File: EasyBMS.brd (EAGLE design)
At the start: 49 x 100 mm, 146 parts, among them Q10 BSS84LT1G, Q11 BSS84LT1G, Q12 BSS84LT1G, Q13 BSS84LT1G, Q2 BSS84LT1G, Q3 BSS84LT1G, Q4 BSS84LT1G, Q5 BSS84LT1G, Q6 BSS84LT1G, Q7 BSS84LT1G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

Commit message: restructured layout
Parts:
- removed JP6: (no value), pinhead:1X08
- added JP10, JP9: (no value), pinhead:1X02
- added JP8: (no value), pinhead:1X05
- JP4: device pinhead:1X08 -> pinhead:1X05
- moved JP4 60.4 mm to (-1.52, -3.81), turned to 0 degrees
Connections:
- removed net GPIO2: JP5.26
- removed net GPIO3: JP5.24
- new net ISIGNAL: JP5.24, JP8.3
- new net N$15: JP4.2
- new net N$17: JP4.3
- new net N$18: JP4.4
- new net N$25: JP4.5
- new net N$7: JP4.1
- net 5VDC: now also JP8.1, JP8.2
- net GND: now also JP10.1, JP10.2, JP8.4, JP8.5, JP9.1, JP9.2
- net GPIO1: no longer JP5.28
- net VTEMP1: now also JP5.28
- net VTEMP2: now also JP5.26

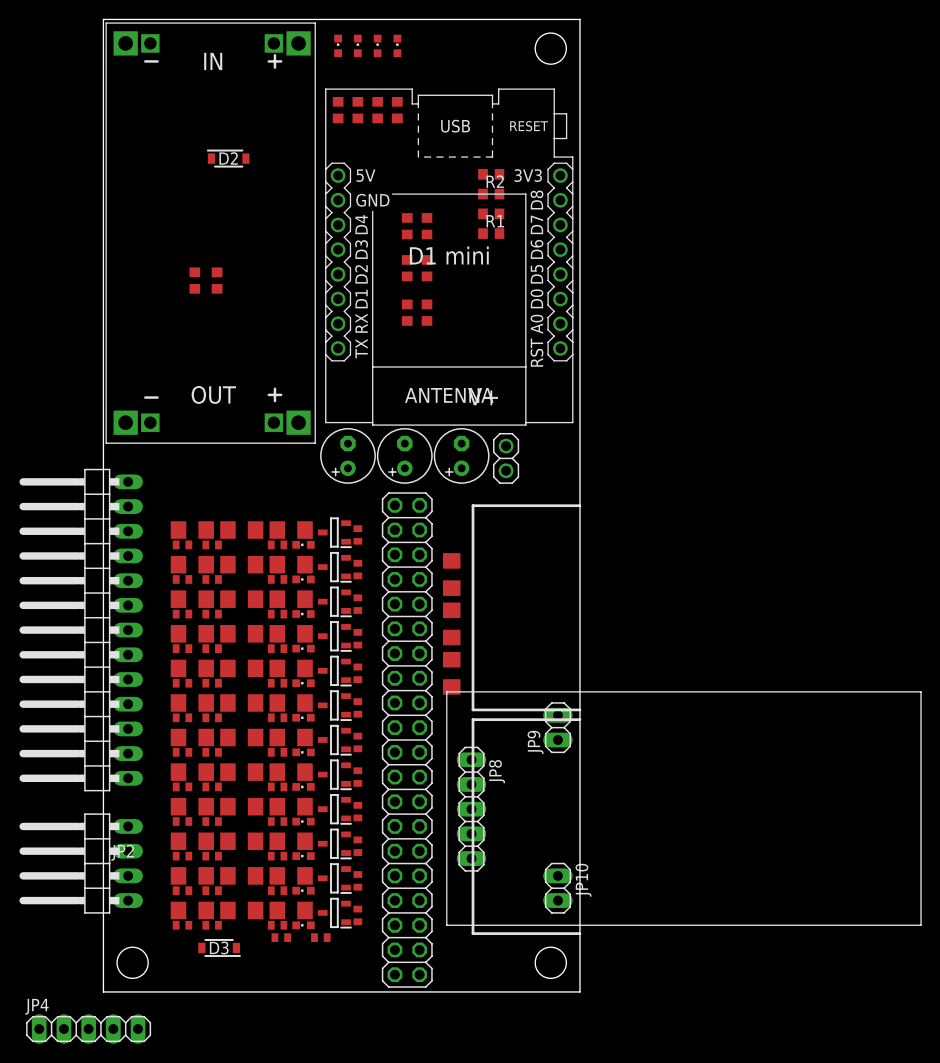
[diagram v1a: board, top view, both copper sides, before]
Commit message: new footprint for current sensor added
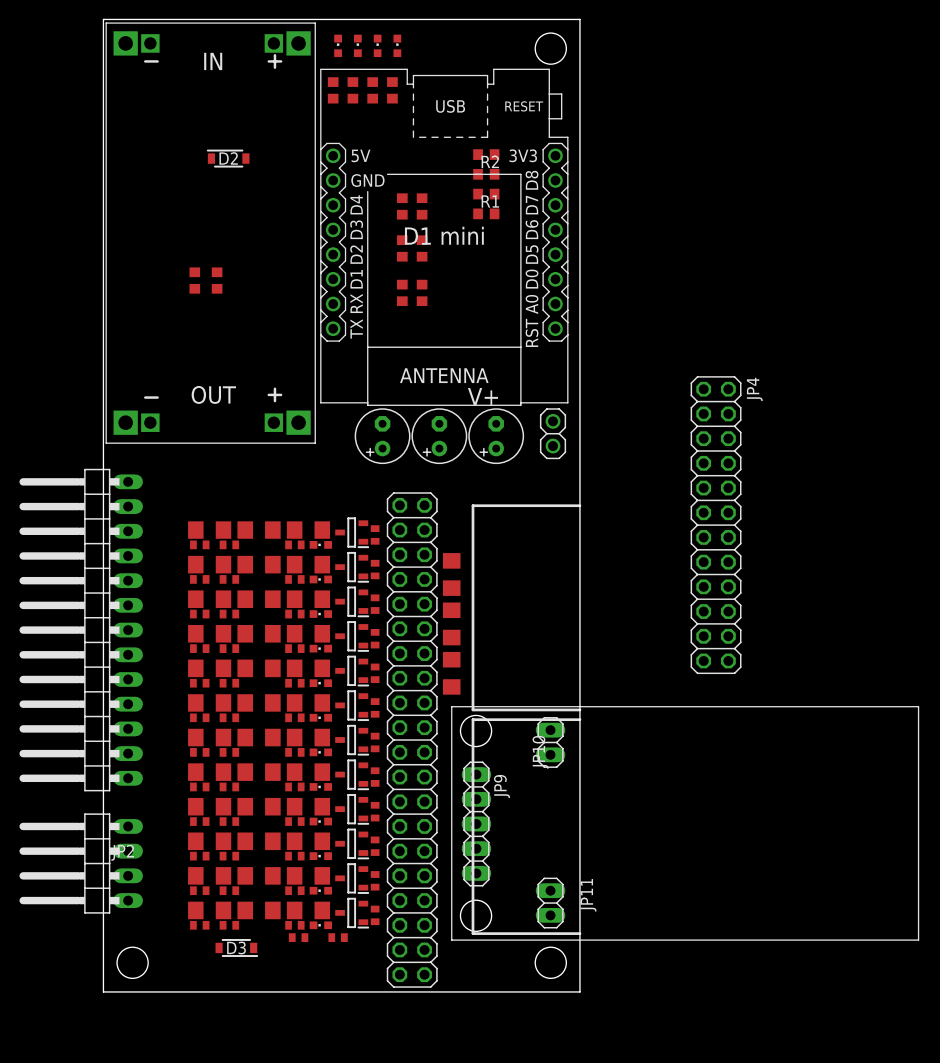
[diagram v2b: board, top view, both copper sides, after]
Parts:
- removed JP8: (no value), pinhead:1X05
- added JP11: (no value), pinhead:1X02
- JP4: device pinhead:1X05 -> pinhead:2X12
- JP9: device pinhead:1X02 -> pinhead:1X05
- moved JP4 82.7 mm to (63.0, 48.0), turned to 270 degrees
- moved JP10 15.0 mm to (46.0, 25.7), turned to 90 degrees
- moved JP9 13.0 mm to (38.4, 17.3), turned to 270 degrees
- moved JP3 5.45 mm to (46.2, 57.4)
- moved C3 4.10 mm to (40.4, 57.1)
- moved C1 4.10 mm to (28.7, 57.1)
- moved C2 4.10 mm to (34.5, 57.1)
- moved R1 2.09 mm to (39.4, 80.0)
- moved R15 2.09 mm to (32.8, 80.8)
- moved R5 2.09 mm to (32.8, 71.9)
- moved U$2 2.09 mm to (35.1, 77.7)
- moved R16 2.09 mm to (30.7, 80.8)
- moved R6 2.09 mm to (30.7, 71.9)
- moved R2 2.09 mm to (39.4, 84.1)
- moved R60 2.09 mm to (32.8, 76.5)
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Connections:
- removed net N$15: JP4.2
- removed net N$17: JP4.3
- removed net N$18: JP4.4
- removed net N$25: JP4.5
- removed net N$7: JP4.1
- net 5VDC: now also JP9.1, JP9.2; no longer JP8.1, JP8.2
- net GND: now also JP11.1, JP11.2, JP9.4, JP9.5; no longer JP8.4, JP8.5, JP9.1, JP9.2
- net ISIGNAL: now also JP9.3; no longer JP8.3

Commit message: layout finished
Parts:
- removed R5: 100R, rcl:R0603
- removed R59: 300k, rcl:R0603
- removed R6: 20k, rcl:R0603
- removed R60: 27k, rcl:R0603
- added C20: 100n, rcl:C0402
- added JP6: (no value), pinhead:2X05
- added R9: 100R, rcl:R0402
- C10, C11, C12, C13, C14, C15, C16, C17, C5, C6, C7, C8, C9: value (none) -> 10nF
- C18, C19, C4: value (none) -> 100nF
- JP4: device pinhead:2X12 -> pinhead:2X05
- R15: value 510k -> 470k
- moved JP2 37.1 mm to (-1.27, 50.3)
- moved JP3 31.5 mm to (15.0, 53.6), turned to 0 degrees
- moved JP4 17.9 mm to (45.2, 49.8)
- moved R58 16.0 mm to (9.65, 57.1)
- moved R57 16.0 mm to (11.7, 57.1)
- moved JP1 11.2 mm to (-1.27, 26.0)
- moved R15 7.37 mm to (37.8, 75.4)
- moved R16 7.37 mm to (35.8, 75.4)
- moved R53 6.35 mm to (30.0, 92.7)
- moved LED4 6.35 mm to (23.9, 97.3)
- moved LED1 5.84 mm to (30.0, 97.3)
- moved R56 5.84 mm to (23.9, 92.7)
- moved R3 3.78 mm to (20.6, 4.32), turned to 0 degrees
- moved R48 3.54 mm to (9.65, 23.4)
- moved R83 3.54 mm to (9.65, 37.6)
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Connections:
- removed net BAT+: R15.2, R59.2
- removed net GPIO1: R59.1, R60.2
- removed net ICMP: R6.1
- removed net IMB: R5.2
- removed net IPB: R5.1
- new net V+: C20.2, JP5.1, R9.1
- net C1: now also JP6.9
- net C10: now also JP4.3
- net C11: now also JP4.1
- net C12: now also JP4.10, JP4.2, JP4.4, JP4.6, JP4.8
- net C2: now also JP6.7
- net C3: now also JP6.5
- net C4: now also JP6.3
- net C5: now also JP6.1
- net C6: now also JP6.10, JP6.2, JP6.4, JP6.6, JP6.8
- net C7: now also JP4.9
- net C8: now also JP4.7
- net C9: now also JP4.5
- net GND: now also C20.1; no longer R6.2, R60.1
- net P13: now also R15.2, R9.2; no longer JP5.1
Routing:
- net P13: track 0.00 -> 148.5 mm, vias 0 -> 3
- net 5VDC: track 0.00 -> 145.4 mm, vias 0 -> 2
- net VTEMP2: track 0.00 -> 75.8 mm, vias 0 -> 3
- net VTEMP1: track 0.00 -> 74.5 mm, vias 0 -> 1
- net C3: track 0.00 -> 72.4 mm, vias 0 -> 1
- net C1: track 0.00 -> 72.0 mm, vias 0 -> 2
- net C2: track 0.00 -> 69.3 mm, vias 0 -> 3
- net VREF2: track 0.00 -> 68.5 mm, vias 0 -> 1
- net C4: track 0.00 -> 66.9 mm, vias 0 -> 2
- net GND: track 0.00 -> 65.1 mm, vias 0 -> 35
- net C5: track 0.00 -> 62.8 mm, vias 0 -> 1
- net C6: track 0.00 -> 61.8 mm, vias 0 -> 1
- net C12: track 0.00 -> 57.0 mm, vias 0 -> 1
- net C7: track 0.00 -> 56.2 mm, vias 0 -> 1
- net C8: track 0.00 -> 55.2 mm, vias 0 -> 1
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- added copper zone on layer 1, net GND
- added copper zone on layer 16, net GND

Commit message: layout changes
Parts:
- moved R3 4.02 mm to (16.8, 3.05), turned to 180 degrees
- moved C20 0.25 mm to (24.4, 51.6)
- moved C18 0.25 mm to (37.3, 37.6)
- moved C4 0.25 mm to (37.3, 32.5)
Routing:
- net C0: track 54.3 -> 29.3 mm
- net C1: track 72.0 -> 70.0 mm
- net S1: track 17.9 -> 19.6 mm
- net VTEMP2: track 75.8 -> 74.2 mm
- net C5: track 62.8 -> 64.3 mm
- net S7: track 12.4 -> 11.1 mm
- net S2: track 10.9 -> 12.0 mm
- net C4: track 66.9 -> 68.0 mm
- net S8: track 10.6 -> 9.54 mm
- net S9: track 9.30 -> 8.33 mm
- net C2: track 69.3 -> 70.3 mm
- net C6: track 61.8 -> 61.0 mm
- net S3: track 17.1 -> 17.8 mm
- net VREF2: track 68.5 -> 69.1 mm
- net S6: track 13.2 -> 12.7 mm
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
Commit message: new branch for meb
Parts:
- added JP22, JP23, JP24, JP25, JP26, JP27, JP28, JP29, JP30, JP31, JP32, JP33, JP34, JP35, JP36: (no value), pinhead_own:1X02
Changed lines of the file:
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@@
 <setting verticaltext="up"/>
 </settings>
-<grid distance="10" unitdist="mil" unit="mil" style="lines" multiple="1" display="yes" altdistance="5" altunitdist="mil" altunit="mil"/>
+<grid distance="1" unitdist="mm" unit="mm" style="lines" multiple="1" display="yes" altdistance="5" altunitdist="mil" altunit="mil"/>
 <layers>
 <layer number="1" name="Top" color="4" fill="1" visible="yes" active="yes"/>
@@
 </pass>
 </autorouter>
+<groups>
+<board_group name="STECKER"/>
+</groups>
 <elements>
 <element name="U$1" library="diy-modules" package="DC-DC-STEP-DOWN-LM2596HVS" value="DC-DC-STEP-DOWN-LM2596HVS" x="2.286" y="97.536" smashed="yes" rot="R270"/>
@@
 <element name="JP10" library="pinhead" library_urn="urn:adsk.eagle:library:325" package="1X02" package3d_urn="urn:adsk.eagle:package:22435/2" value="" x="45.974" y="25.654" smashed="yes" rot="R90">
 <attribute name="NAME" x="45.4152" y="23.0378" size="1.27" layer="25" ratio="10" rot="R90"/>
-<attribute name="POPULARITY" value="98" x="47.244" y="25.654" size="1.778" layer="27" rot="R90" display="off"/>
 <attribute name="VALUE" x="50.419" y="23.114" size="1.27" layer="27" rot="R90"/>
 </element>
 <element name="JP11" library="pinhead" library_urn="urn:adsk.eagle:library:325" package="1X02" package3d_urn="urn:adsk.eagle:package:22435/2" value="" x="45.974" y="9.144" smashed="yes" rot="R270">
 <attribute name="NAME" x="49.0728" y="11.7602" size="1.27" layer="25" ratio="10" rot="R270"/>
-<attribute name="POPULARITY" value="98" x="47.244" y="9.144" size="1.778" layer="27" rot="R270" display="off"/>
 <attribute name="VALUE" x="44.069" y="11.684" size="1.27" layer="27" rot="R270"/>
 </element>
@@
 <attribute name="NAME" x="25.019" y="52.197" size="1.27" layer="25" rot="R270"/>
 <attribute name="VALUE" x="22.479" y="52.197" size="1.27" layer="27" rot="R270"/>
+</element>
+<element name="JP22" library="pinhead_own" package="1X02" package3d_urn="urn:adsk.eagle:package:22435/2" value="" x="-5" y="-68" smashed="yes" rot="R180" grouprefs="STECKER">
+<attribute name="NAME" x="-2.3838" y="-69.8288" size="1.27" layer="25" ratio="10" rot="R180"/>
+<attribute name="VALUE" x="-2.46" y="-64.825" size="1.27" layer="27" rot="R180"/>
+</element>
+<element name="JP23" library="pinhead_own" package="1X02" package3d_urn="urn:adsk.eagle:package:22435/2" value="" x="-5" y="-71" smashed="yes" grouprefs="STECKER">
+<attribute name="NAME" x="-7.6162" y="-69.1712" size="1.27" layer="25" ratio="10"/>
+<attribute name="VALUE" x="-7.54" y="-74.175" size="1.27" layer="27"/>
+</element>
+<element name="JP24" library="pinhead_own" package="1X02" package3d_urn="urn:adsk.eagle:package:22435/2" value="" x="-5" y="-74" smashed="yes" grouprefs="STECKER">
+<attribute name="NAME" x="-7.6162" y="-72.1712" size="1.27" layer="25" ratio="10"/>
+<attribute name="VALUE" x="-7.54" y="-77.175" size="1.27" layer="27"/>
+</element>
+<element name="JP25" library="pinhead_own" package="1X02" package3d_urn="urn:adsk.eagle:package:22435/2" value="" x="-5" y="-77" smashed="yes" grouprefs="STECKER">
+<attribute name="NAME" x="-7.6162" y="-75.1712" size="1.27" layer="25" ratio="10"/>
+<attribute name="VALUE" x="-7.54" y="-80.175" size="1.27" layer="27"/>
+</element>
+<element name="JP26" library="pinhead_own" package="1X02" package3d_urn="urn:adsk.eagle:package:22435/2" value="" x="-5" y="-80" smashed="yes" grouprefs="STECKER">
+<attribute name="NAME" x="-7.6162" y="-78.1712" size="1.27" layer="25" ratio="10"/>
+<attribute name="VALUE" x="-7.54" y="-83.175" size="1.27" layer="27"/>
+</element>
+<element name="JP27" library="pinhead_own" package="1X02" package3d_urn="urn:adsk.eagle:package:22435/2" value="" x="-5" y="-83" smashed="yes" grouprefs="STECKER">
+<attribute name="NAME" x="-7.6162" y="-81.1712" size="1.27" layer="25" ratio="10"/>
+<attribute name="VALUE" x="-7.54" y="-86.175" size="1.27" layer="27"/>
+</element>
+<element name="JP28" library="pinhead_own" package="1X02" package3d_urn="urn:adsk.eagle:package:22435/2" value="" x="-5" y="-86" smashed="yes" grouprefs="STECKER">
+<attribute name="NAME" x="-7.6162" y="-84.1712" size="1.27" layer="25" ratio="10"/>
+<attribute name="VALUE" x="-7.54" y="-89.175" size="1.27" layer="27"/>
+</element>
+<element name="JP29" library="pinhead_own" package="1X02" package3d_urn="urn:adsk.eagle:package:22435/2" value="" x="-5" y="-89" smashed="yes" grouprefs="STECKER">
+<attribute name="NAME" x="-7.6162" y="-87.1712" size="1.27" layer="25" ratio="10"/>
+<attribute name="VALUE" x="-7.54" y="-92.175" size="1.27" layer="27"/>
+</element>
+<element name="JP30" library="pinhead_own" package="1X02" package3d_urn="urn:adsk.eagle:package:22435/2" value="" x="-5" y="-92" smashed="yes" grouprefs="STECKER">
+<attribute name="NAME" x="-7.6162" y="-90.1712" size="1.27" layer="25" ratio="10"/>
+<attribute name="VALUE" x="-7.54" y="-95.175" size="1.27" layer="27"/>
+</element>
+<element name="JP31" library="pinhead_own" package="1X02" package3d_urn="urn:adsk.eagle:package:22435/2" value="" x="-5" y="-95" smashed="yes" grouprefs="STECKER">
+<attribute name="NAME" x="-7.6162" y="-93.1712" size="1.27" layer="25" ratio="10"/>
+<attribute name="VALUE" x="-7.54" y="-98.175" size="1.27" layer="27"/>
+</element>
+<element name="JP32" library="pinhead_own" package="1X02" package3d_urn="urn:adsk.eagle:package:22435/2" value="" x="-5" y="-98" smashed="yes" grouprefs="STECKER">
+<attribute name="NAME" x="-7.6162" y="-96.1712" size="1.27" layer="25" ratio="10"/>
+<attribute name="VALUE" x="-7.54" y="-101.175" size="1.27" layer="27"/>
+</element>
+<element name="JP33" library="pinhead_own" package="1X02" package3d_urn="urn:adsk.eagle:package:22435/2" value="" x="-5" y="-101" smashed="yes" grouprefs="STECKER">
+<attribute name="NAME" x="-7.6162" y="-99.1712" size="1.27" layer="25" ratio="10"/>
+<attribute name="VALUE" x="-7.54" y="-104.175" size="1.27" layer="27"/>
+</element>
+<element name="JP34" library="pinhead_own" package="1X02" package3d_urn="urn:adsk.eagle:package:22435/2" value="" x="-5" y="-144" smashed="yes">
+<attribute name="NAME" x="-7.6162" y="-142.1712" size="1.27" layer="25" ratio="10"/>
+<attribute name="VALUE" x="-7.54" y="-147.175" size="1.27" layer="27"/>
+</element>
+<element name="JP35" library="pinhead_own" package="1X02" package3d_urn="urn:adsk.eagle:package:22435/2" value="" x="-5" y="-150" smashed="yes">
+<attribute name="NAME" x="-7.6162" y="-148.1712" size="1.27" layer="25" ratio="10"/>
+<attribute name="VALUE" x="-7.54" y="-153.175" size="1.27" layer="27"/>
+</element>
+<element name="JP36" library="pinhead_own" package="1X02" package3d_urn="urn:adsk.eagle:package:22435/2" value="" x="-5" y="-156" smashed="yes">
+<attribute name="NAME" x="-7.6162" y="-154.1712" size="1.27" layer="25" ratio="10"/>
+<attribute name="VALUE" x="-7.54" y="-159.175" size="1.27" layer="27"/>
 </element>
 </elements>
@@
 packages will not be understood (or retained) with this version.
 </note>
+<note version="9.5" severity="warning">
+Since Version 9.5, EAGLE supports persistent groups with
+schematics, and board files. Those persistent groups
+will not be understood (or retained) with this version.
+</note>
 </compatibility>

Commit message: MEB parts placed
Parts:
- removed JP1: (no value), pinhead:1X13/90
- removed JP2: (no value), pinhead:1X04/90
- removed JP22, JP23, JP24, JP25, JP26, JP27, JP28, JP29, JP30, JP31, JP32, JP33, JP34, JP35, JP36: (no value), pinhead_own:1X02
- removed JP4, JP6: (no value), pinhead:2X05
- added H1, H2, H3: MOUNT-HOLE3.2, holes:3,2
- added JP7: (no value), pinhead_own:2X11_MEB12S
- moved R57 9.92 mm to (2.03, 54.9), turned to 0 degrees
- moved R58 8.76 mm to (2.03, 52.8), turned to 0 degrees
- moved C10 2.90 mm to (9.40, 20.6)
- moved C11 2.90 mm to (9.40, 24.1)
- moved C12 2.90 mm to (9.40, 27.7)
- moved C13 2.90 mm to (9.40, 31.2)
- moved C14 2.90 mm to (9.40, 34.8)
- moved C15 2.90 mm to (9.40, 38.4)
- moved C17 2.90 mm to (9.40, 45.5)
- moved C7 2.90 mm to (9.40, 9.91)
- moved C8 2.90 mm to (9.40, 17.0)
- moved C9 2.90 mm to (9.40, 13.5)
- moved LED11 2.90 mm to (21.8, 24.1)
- moved LED12 2.90 mm to (21.8, 27.7)
- moved LED13 2.90 mm to (21.8, 31.2)
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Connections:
- removed net P10: C15.2, JP1.10, Q10.2, R76.2, R77.1, R81.2
- removed net P11: C16.2, JP1.11, Q11.2, R83.2, R84.1, R88.2
- removed net P12: C17.2, JP1.12, Q12.2, R89.2, R90.1, R94.2
- removed net P13: D2.1, JP1.13, Q13.2, R15.2, R9.2, R95.2, U$1.IN+
- removed net P2: C7.2, D3.1, JP1.2, Q2.2, R12.2, R14.1, R23.2
- removed net P3: C9.2, JP1.3, Q3.2, R24.2, R31.1, R35.2
- removed net P4: C8.2, JP1.4, Q5.2, R25.1, R29.2, R36.2
- removed net P5: C10.2, JP1.5, Q4.2, R30.2, R37.1, R41.2
- removed net P6: C11.2, JP1.6, Q6.2, R42.2, R43.1, R47.2
- removed net P7: C12.2, JP1.7, Q7.2, R48.2, R49.1, R63.2
- removed net P8: C13.2, JP1.8, Q8.2, R64.2, R65.1, R69.2
- removed net P9: C14.2, JP1.9, Q9.2, R70.2, R71.1, R75.2
- new net C1+: C7.2, D3.1, JP7.16_C1+, Q2.2, R12.2, R14.1, R23.2
- new net C1-: C5.2, C6.2, D3.2, JP7.15_TOTAL-, R11.2, R3.2, R4.1
- new net C10+: C16.2, JP7.3_C10+, Q11.2, R83.2, R84.1, R88.2
- new net C11+: C17.2, JP7.4_C11+, Q12.2, R89.2, R90.1, R94.2
- new net C12+: JP7.2_TOTAL+2, Q13.2, R95.2
- new net C2+: C9.2, JP7.13_C2+, Q3.2, R24.2, R31.1, R35.2
- new net C3+: C8.2, JP7.14_C3+, Q5.2, R25.1, R29.2, R36.2
- new net C4+: C10.2, JP7.11_C4+, Q4.2, R30.2, R37.1, R41.2
- new net C5+: C11.2, JP7.10_C5+, Q6.2, R42.2, R43.1, R47.2
- new net C6+: C12.2, JP7.7_C6+, Q7.2, R48.2, R49.1, R63.2
- new net C7+: C13.2, JP7.8_C7+, Q8.2, R64.2, R65.1, R69.2
- new net C8+: C14.2, JP7.5_C8+, Q9.2, R70.2, R71.1, R75.2
- new net C9+: C15.2, JP7.6_C9+, Q10.2, R76.2, R77.1, R81.2
- new net GNDPOWER: JP7.17_TOTAL-
- new net VIN: D2.1, JP7.1_TOTAL+, R15.2, R9.2, U$1.IN+
- net C1: no longer JP6.9
- net C10: no longer JP4.3
- net C11: no longer JP4.1
- net C12: no longer JP4.10, JP4.2, JP4.4, JP4.6, JP4.8
- net C2: no longer JP6.7
- net C3: no longer JP6.5
- net C4: no longer JP6.3
- net C5: no longer JP6.1
- net C6: no longer JP6.10, JP6.2, JP6.4, JP6.6, JP6.8
- net C7: no longer JP4.9
- net C8: no longer JP4.7
- net C9: no longer JP4.5
- net GND: no longer C5.2, C6.2, D3.2, JP1.1, R11.2, R3.2, R4.1
- net VREF2: now also JP7.19_THERMO1_IN, JP7.20_THERMO2_IN; no longer JP2.1, JP2.3
- net VTEMP1: now also JP7.21_THERMO1_OUT; no longer JP2.2
- net VTEMP2: now also JP7.22_THERMO2_OUT; no longer JP2.4
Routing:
- net P13: track 148.5 -> 0.00 mm, vias 3 -> 0
- net VIN: track 0.00 -> 98.3 mm, vias 0 -> 3
- net C1+: track 0.00 -> 59.2 mm, vias 0 -> 3
- net C2+: track 0.00 -> 50.5 mm, vias 0 -> 3
- net C3+: track 0.00 -> 49.9 mm, vias 0 -> 2
- net C6+: track 0.00 -> 49.8 mm, vias 0 -> 3
- net C8+: track 0.00 -> 48.5 mm, vias 0 -> 2
- net C5+: track 0.00 -> 48.3 mm, vias 0 -> 2
- net C11+: track 0.00 -> 46.9 mm, vias 0 -> 2
- net C4+: track 0.00 -> 45.6 mm, vias 0 -> 2
- net C7+: track 0.00 -> 45.0 mm, vias 0 -> 2
- net C1-: track 0.00 -> 43.9 mm
- net C9+: track 0.00 -> 43.5 mm, vias 0 -> 2
- net C1: track 70.0 -> 29.7 mm, vias 2 -> 1
- net C10+: track 0.00 -> 39.0 mm, vias 0 -> 2
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
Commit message: review of layout #1
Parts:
- added R5, R6: 1k, rcl:R0603
- moved R57 54.7 mm to (20.3, 3.30), turned to 90 degrees
- moved R58 53.6 mm to (22.6, 3.30), turned to 90 degrees
- moved JP3 30.5 mm to (45.2, 57.4)
- moved R61 8.41 mm to (43.4, 78.7)
- moved R2 4.60 mm to (38.9, 79.5), turned to 180 degrees
- moved R62 4.26 mm to (43.4, 81.3)
- moved H3 1.44 mm to (45.0, 96.0)
- moved H1 1.44 mm to (4.02, 4.02)
- moved H2 1.44 mm to (45.0, 4.02)
- moved R1 0.72 mm to (38.9, 81.5), turned to 180 degrees
- moved D2 0.51 mm to (12.9, 86.2)
- moved LED1 0.51 mm to (30.0, 97.8)
- moved LED2 0.51 mm to (27.9, 97.8)
- moved LED3 0.51 mm to (25.9, 97.8)
- moved LED4 0.51 mm to (23.9, 97.8)
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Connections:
- new net N$15: R6.1, U$2.JP1.7
- new net N$7: R5.1, U$2.JP1.4
- net CSB: now also R6.2; no longer U$2.JP1.7
- net SCK: now also R5.2; no longer U$2.JP1.4
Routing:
- net VTEMP2: track 108.4 -> 48.9 mm, vias 0 -> 1
- net VTEMP1: track 99.6 -> 40.8 mm
- net GND: track 48.1 -> 18.8 mm, vias 0 -> 183
- net N$5: track 36.7 -> 11.6 mm, vias 1 -> 0
- net N$6: track 46.6 -> 21.4 mm, vias 1 -> 0
- net MISO: track 47.6 -> 36.6 mm
- net N$73: track 10.3 -> 2.25 mm, vias 1 -> 0
- net C3: track 43.6 -> 36.8 mm
- net C2: track 40.4 -> 35.6 mm
- net N$119: track 6.63 -> 2.25 mm
- net CSB: track 51.9 -> 47.6 mm, vias 0 -> 2
- net MOSI: track 44.9 -> 41.2 mm, vias 1 -> 2
- net N$7: track 0.00 -> 2.25 mm
- net N$15: track 0.00 -> 2.25 mm
- net SCK: track 36.0 -> 34.8 mm, vias 1 -> 2
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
